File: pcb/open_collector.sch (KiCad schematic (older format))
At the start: 38 parts, among them Q1 BC817, Q2 BC817, Q3 BC817, Q4 BC817, Q5 BC817, Q6 BC817

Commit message: testpoints footprints added, some footprints assigned
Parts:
- R10, R11, R12, R13, R14, R15, R16, R17, R18, R19, R20, R7, R8, R9: footprint (none) -> Resistor_SMD:R_0603_1608Metric_Pad1.05x0.95mm_HandSolder
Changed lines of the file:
@@
 F 0 "R18" V 7843 1850 50  0000 C CNN
 F 1 "1k" V 7934 1850 50  0000 C CNN
-F 2 "" V 7980 1850 50  0001 C CNN
+F 2 "Resistor_SMD:R_0603_1608Metric_Pad1.05x0.95mm_HandSolder" V 7980 1850 50  0001 C CNN
 F 3 "~" H 8050 1850 50  0001 C CNN
 	1    8050 1850
@@
 F 0 "R17" V 7793 3850 50  0000 C CNN
 F 1 "1k" V 7884 3850 50  0000 C CNN
-F 2 "" V 7930 3850 50  0001 C CNN
+F 2 "Resistor_SMD:R_0603_1608Metric_Pad1.05x0.95mm_HandSolder" V 7930 3850 50  0001 C CNN
 F 3 "~" H 8000 3850 50  0001 C CNN
 	1    8000 3850
@@
 F 0 "R15" H 7670 3596 50  0000 L CNN
 F 1 "4.7k" H 7670 3505 50  0000 L CNN
-F 2 "" V 7530 3550 50  0001 C CNN
+F 2 "Resistor_SMD:R_0603_1608Metric_Pad1.05x0.95mm_HandSolder" V 7530 3550 50  0001 C CNN
 F 3 "~" H 7600 3550 50  0001 C CNN
 	1    7600 3550
@@
 F 0 "R7" V 2293 1500 50  0000 C CNN
 F 1 "1k" V 2384 1500 50  0000 C CNN
-F 2 "" V 2430 1500 50  0001 C CNN
+F 2 "Resistor_SMD:R_0603_1608Metric_Pad1.05x0.95mm_HandSolder" V 2430 1500 50  0001 C CNN
 F 3 "~" H 2500 1500 50  0001 C CNN
 	1    2500 1500
@@
 F 0 "R11" H 2970 1796 50  0000 L CNN
 F 1 "1k" H 2970 1705 50  0000 L CNN
-F 2 "" V 2830 1750 50  0001 C CNN
+F 2 "Resistor_SMD:R_0603_1608Metric_Pad1.05x0.95mm_HandSolder" V 2830 1750 50  0001 C CNN
 F 3 "~" H 2900 1750 50  0001 C CNN
 	1    2900 1750
@@
 F 0 "R8" V 2293 3000 50  0000 C CNN
 F 1 "1k" V 2384 3000 50  0000 C CNN
-F 2 "" V 2430 3000 50  0001 C CNN
+F 2 "Resistor_SMD:R_0603_1608Metric_Pad1.05x0.95mm_HandSolder" V 2430 3000 50  0001 C CNN
 F 3 "~" H 2500 3000 50  0001 C CNN
 	1    2500 3000
@@
 F 0 "R12" H 2970 3296 50  0000 L CNN
 F 1 "1k" H 2970 3205 50  0000 L CNN
-F 2 "" V 2830 3250 50  0001 C CNN
+F 2 "Resistor_SMD:R_0603_1608Metric_Pad1.05x0.95mm_HandSolder" V 2830 3250 50  0001 C CNN
 F 3 "~" H 2900 3250 50  0001 C CNN
 	1    2900 3250
@@
 F 0 "R9" V 2293 4500 50  0000 C CNN
 F 1 "1k" V 2384 4500 50  0000 C CNN
-F 2 "" V 2430 4500 50  0001 C CNN
+F 2 "Resistor_SMD:R_0603_1608Metric_Pad1.05x0.95mm_HandSolder" V 2430 4500 50  0001 C CNN
 F 3 "~" H 2500 4500 50  0001 C CNN
 	1    2500 4500
@@
 F 0 "R13" H 2970 4796 50  0000 L CNN
 F 1 "1k" H 2970 4705 50  0000 L CNN
-F 2 "" V 2830 4750 50  0001 C CNN
+F 2 "Resistor_SMD:R_0603_1608Metric_Pad1.05x0.95mm_HandSolder" V 2830 4750 50  0001 C CNN
 F 3 "~" H 2900 4750 50  0001 C CNN
 	1    2900 4750
@@
 F 0 "R10" V 2293 6000 50  0000 C CNN
 F 1 "1k" V 2384 6000 50  0000 C CNN
-F 2 "" V 2430 6000 50  0001 C CNN
+F 2 "Resistor_SMD:R_0603_1608Metric_Pad1.05x0.95mm_HandSolder" V 2430 6000 50  0001 C CNN
 F 3 "~" H 2500 6000 50  0001 C CNN
 	1    2500 6000
@@
 F 0 "R14" H 2970 6296 50  0000 L CNN
 F 1 "1k" H 2970 6205 50  0000 L CNN
-F 2 "" V 2830 6250 50  0001 C CNN
+F 2 "Resistor_SMD:R_0603_1608Metric_Pad1.05x0.95mm_HandSolder" V 2830 6250 50  0001 C CNN
 F 3 "~" H 2900 6250 50  0001 C CNN
 	1    2900 6250
@@
 F 0 "R19" H 8520 2146 50  0000 L CNN
 F 1 "1k" H 8520 2055 50  0000 L CNN
-F 2 "" V 8380 2100 50  0001 C CNN
+F 2 "Resistor_SMD:R_0603_1608Metric_Pad1.05x0.95mm_HandSolder" V 8380 2100 50  0001 C CNN
 F 3 "~" H 8450 2100 50  0001 C CNN
 	1    8450 2100
@@
 F 0 "R16" H 7720 1646 50  0000 L CNN
 F 1 "4.7k" H 7720 1555 50  0000 L CNN
-F 2 "" V 7580 1600 50  0001 C CNN
+F 2 "Resistor_SMD:R_0603_1608Metric_Pad1.05x0.95mm_HandSolder" V 7580 1600 50  0001 C CNN
 F 3 "~" H 7650 1600 50  0001 C CNN
 	1    7650 1600
@@
 F 0 "R20" H 8520 4146 50  0000 L CNN
 F 1 "1k" H 8520 4055 50  0000 L CNN
-F 2 "" V 8380 4100 50  0001 C CNN
+F 2 "Resistor_SMD:R_0603_1608Metric_Pad1.05x0.95mm_HandSolder" V 8380 4100 50  0001 C CNN
 F 3 "~" H 8450 4100 50  0001 C CNN
 	1    8450 4100

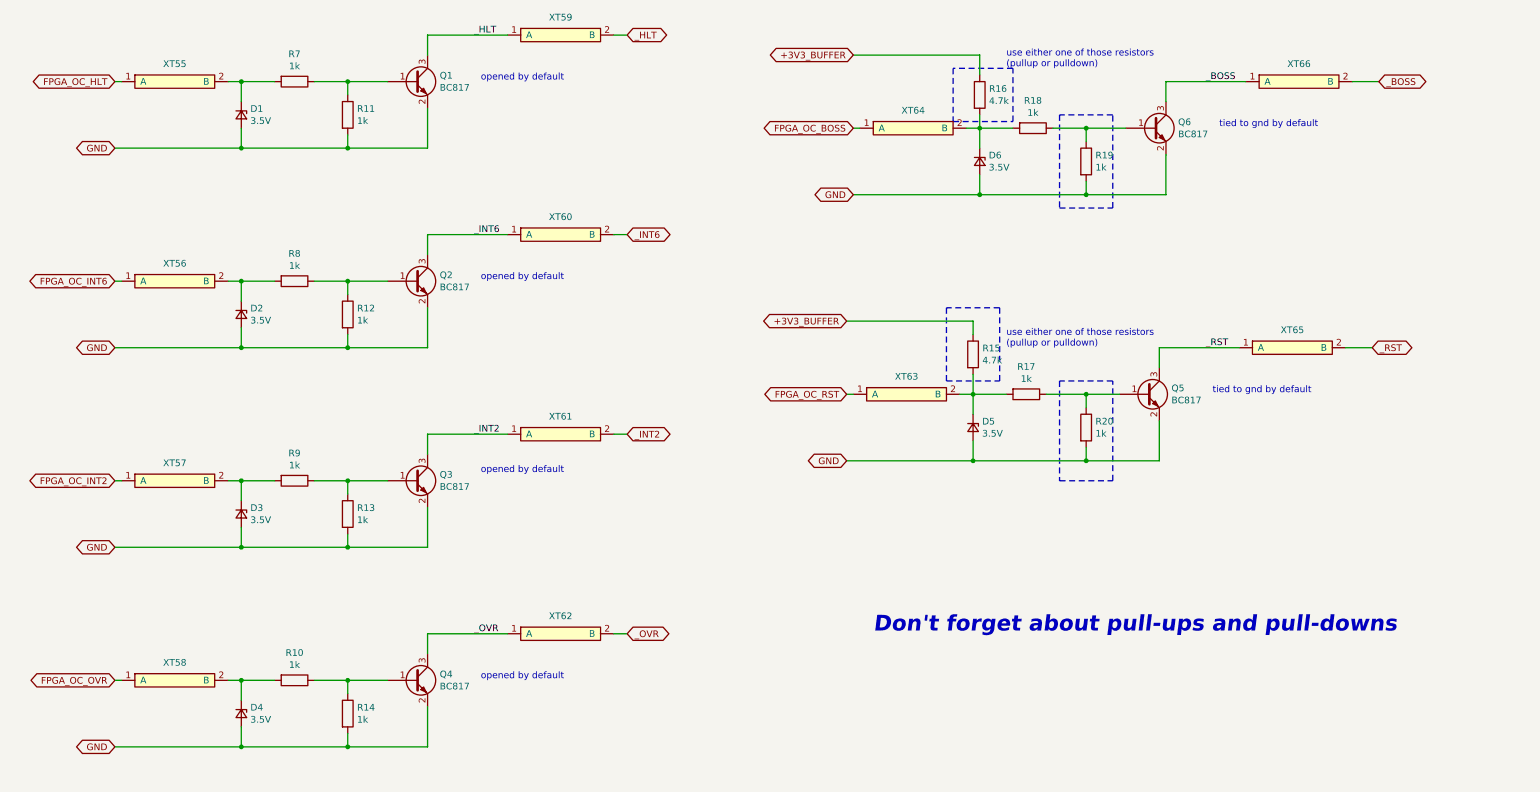
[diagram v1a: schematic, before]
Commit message: more footprints assigned
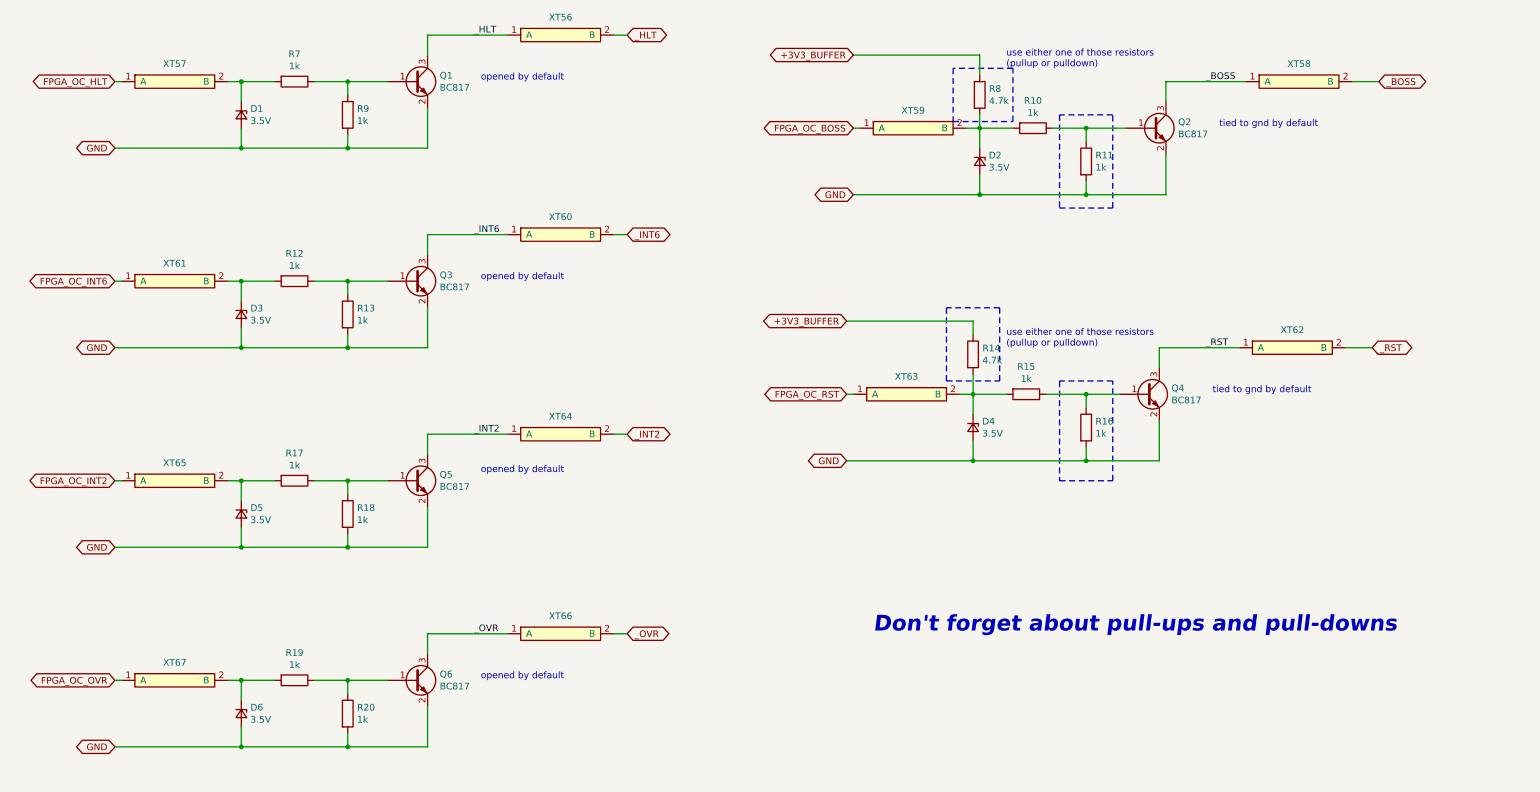
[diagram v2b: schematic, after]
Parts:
- XT56: renamed from XT59; footprint (none) -> WM1200:testpoint_cutline
- XT57: renamed from XT55; footprint (none) -> WM1200:testpoint_cutline
- XT58: renamed from XT66; footprint (none) -> WM1200:testpoint_cutline
- XT59: renamed from XT64; footprint (none) -> WM1200:testpoint_cutline
- XT60, XT63: footprint (none) -> WM1200:testpoint_cutline
- XT61: renamed from XT56; footprint (none) -> WM1200:testpoint_cutline
- XT62: renamed from XT65; footprint (none) -> WM1200:testpoint_cutline
- XT64: renamed from XT61; footprint (none) -> WM1200:testpoint_cutline
- XT65: renamed from XT57; footprint (none) -> WM1200:testpoint_cutline
- XT66: renamed from XT62; footprint (none) -> WM1200:testpoint_cutline
- XT67: renamed from XT58; footprint (none) -> WM1200:testpoint_cutline
- renumbered D6 to D2, D2 to D3, D5 to D4, D3 to D5, D4 to D6, Q6 to Q2, Q2 to Q3, Q5 to Q4, Q3 to Q5, Q4 to Q6, R18 to R10, R19 to R11, R8 to R12, R12 to R13, R15 to R14, R17 to R15, R20 to R16, R9 to R17, R13 to R18, R10 to R19, R14 to R20, R16 to R8, R11 to R9

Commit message: more footprints assigned, caps added into open collector base circuit
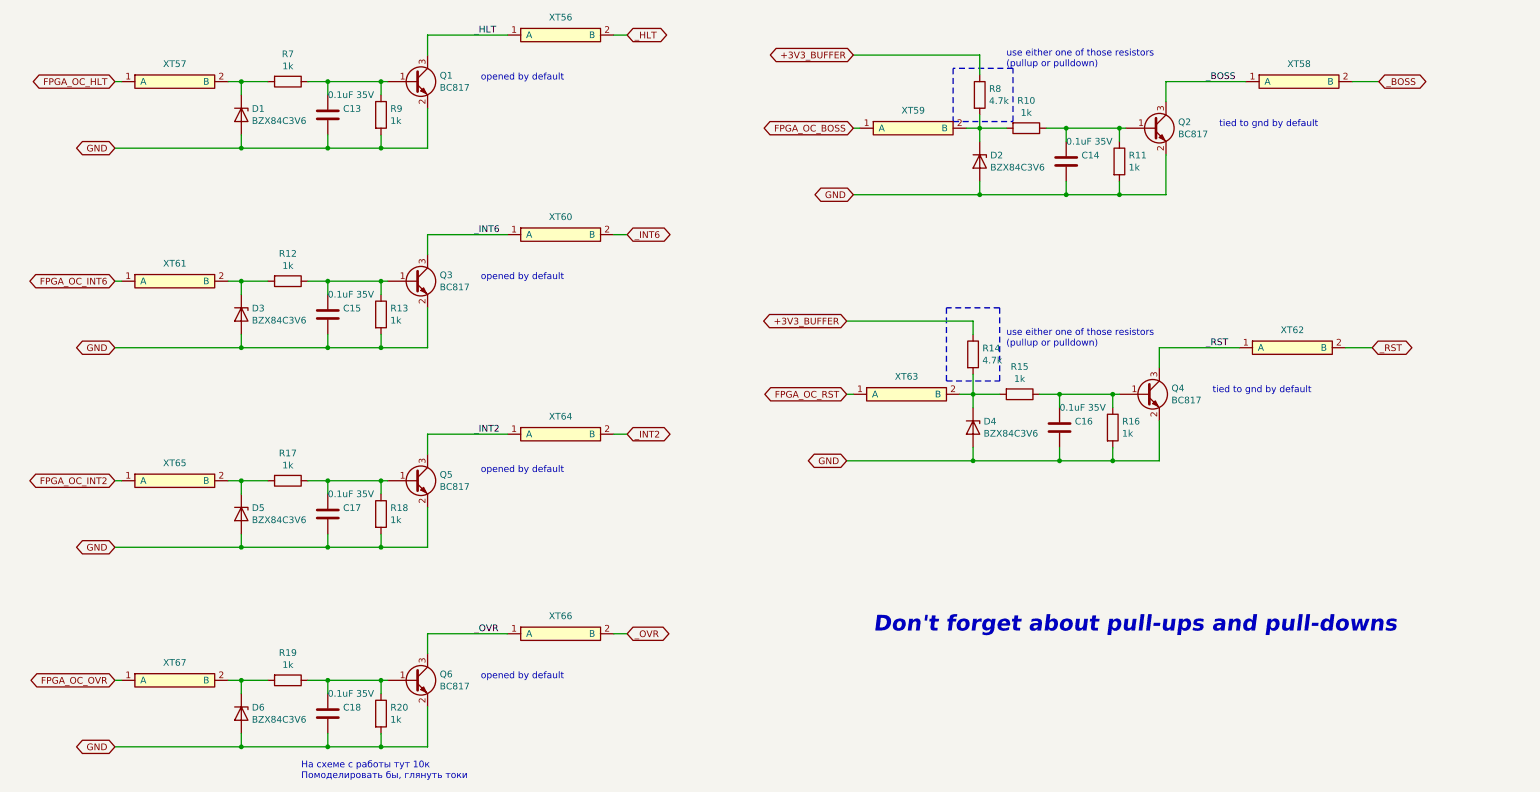
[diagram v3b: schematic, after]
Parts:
- removed D1, D2, D3, D4, D5, D6: 3.5V, symbol Device:D_Zener_Small
- added C13, C14, C15, C16, C17, C18: 0.1uF 35V, Capacitor_SMD:C_0603_1608Metric_Pad1.05x0.95mm_HandSolder, symbol Device:C
- added D1, D2, D3, D4, D5, D6: BZX84C3V6, Diode_SMD:D_SOT-23_ANK, symbol Diode:BZX84Cxx
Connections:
- net GND: now also C13.1, C14.1, C15.1, C16.1, C17.1, C18.1, D1.2 (A), D2.2 (A), D3.2 (A), D4.2 (A), D5.2 (A), D6.2 (A)
- net at Q4.1 (B), R15.1, R16.1: now also C16.2
- net at Q2.1 (B), R10.1, R11.1: now also C14.2
- net at Q1.1 (B), R7.1, R9.1: now also C13.2
- net at Q3.1 (B), R12.1, R13.1: now also C15.2
- net at Q5.1 (B), R17.1, R18.1: now also C17.2
- net at Q6.1 (B), R19.1, R20.1: now also C18.2
- net at R19.2, XT67.2 (B): now also D6.1 (K)
- net at R17.2, XT65.2 (B): now also D5.1 (K)
- net at R12.2, XT61.2 (B): now also D3.1 (K)
- net at R7.2, XT57.2 (B): now also D1.1 (K)
- net at R14.2, R15.2, XT63.2 (B): now also D4.1 (K)
- net at R10.2, R8.2, XT59.2 (B): now also D2.1 (K)
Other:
- note added: "На схеме с работы тут 10к\nПомоделировать бы, глянуть токи"
- moved on the sheet: R10, R11, R12, R13, R15, R16, R17, R18, R19, R20, R7, R9

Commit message: Board pcb updated
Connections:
- net _BOSS: no longer Q2.3 (C), XT58.1 (A)
- net _HLT: no longer Q1.3 (C), XT56.1 (A)
- net _INT2: no longer Q5.3 (C), XT64.1 (A)
- net _INT6: no longer Q3.3 (C), XT60.1 (A)
- net _OVR: no longer Q6.3 (C), XT66.1 (A)
- net _RST: no longer Q4.3 (C), XT62.1 (A)
- new net: Q6.3 (C), XT66.1 (A)
- new net: Q5.3 (C), XT64.1 (A)
- new net: Q3.3 (C), XT60.1 (A)
- new net: Q1.3 (C), XT56.1 (A)
- new net: Q4.3 (C), XT62.1 (A)
- new net: Q2.3 (C), XT58.1 (A)
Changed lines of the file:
@@
 Wire Wire Line
 	2100 6500 1150 6500
-Text Label 9350 1500 0    50   ~ 0
-_BOSS
-Text Label 9350 3500 0    50   ~ 0
-_RST
-Text Label 3850 1150 0    50   ~ 0
-_HLT
-Text Label 3850 2650 0    50   ~ 0
-_INT6
-Text Label 3850 4150 0    50   ~ 0
-_INT2
-Text Label 3850 5650 0    50   ~ 0
-_OVR
 Text GLabel 6700 2350 0    50   BiDi ~ 0
 GND

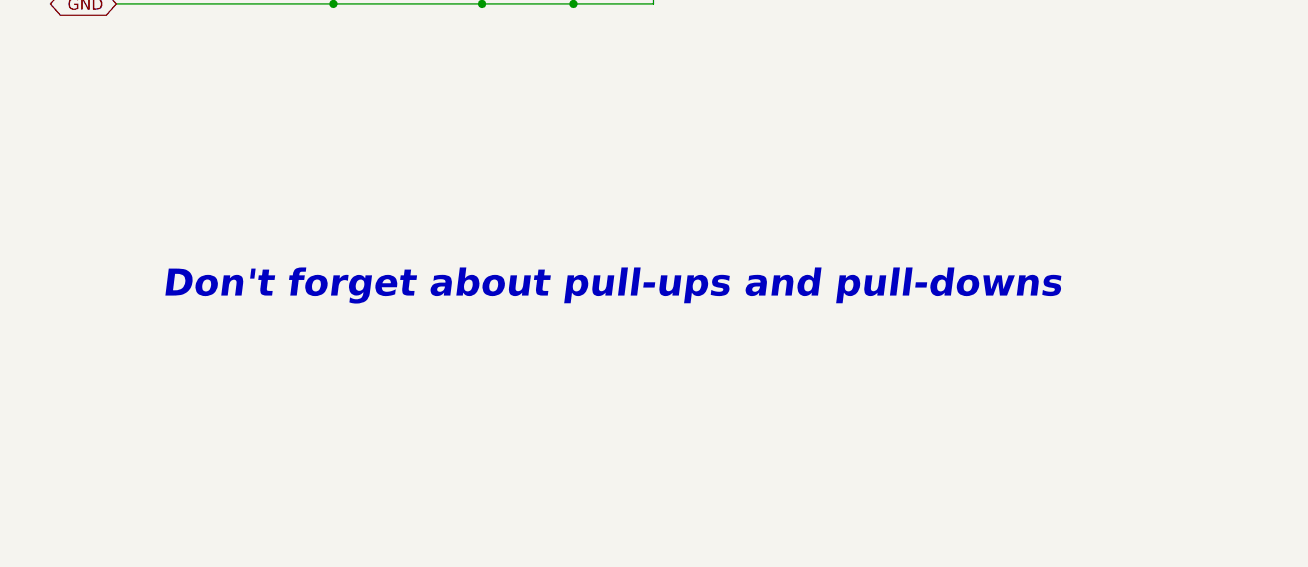
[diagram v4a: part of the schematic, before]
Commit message: SCH comments updated
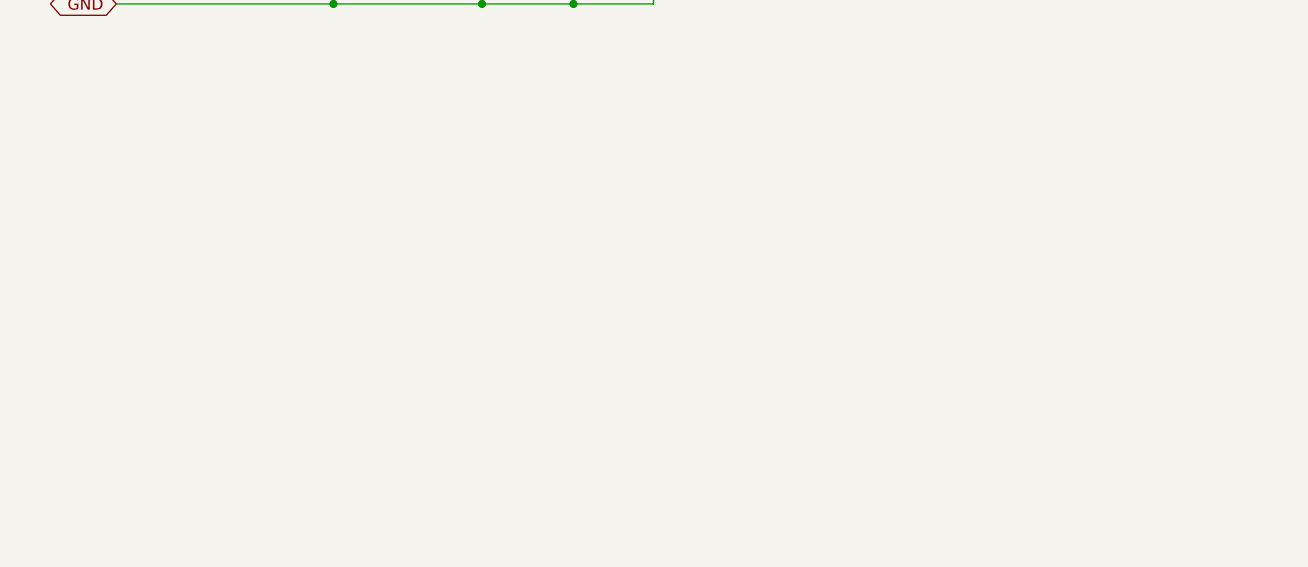
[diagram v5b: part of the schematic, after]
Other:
- note removed: "Don't forget about pull-ups and pull-downs"
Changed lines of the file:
@@
 $Descr A4 11693 8268
 encoding utf-8
-Sheet 10 12
-Title "WishMaster 1200"
+Sheet 9 11
+Title "Wishmaster 1200"
 Date ""
 Rev "ES1"
-Comp "Konfusion"
+Comp "Created by Konfusion in 2020"
 Comment1 "A1200 version (engineering prototype)"
 Comment2 "Wishmaster ARM \\ JIT turbo board for Amiga"
@@
 	2000 6000 2100 6000
 Connection ~ 2100 6000
-Text Notes 6850 5650 0    118  Italic 24
-Don't forget about pull-ups and pull-downs
 Text GLabel 10650 1500 2    50   BiDi ~ 0
 _BOSS
